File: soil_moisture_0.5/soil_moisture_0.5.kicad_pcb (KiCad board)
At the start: 2 copper layers, 10 parts, among them J1 PPTC021LFBN-RC, J2 1725698, Q1 FDP7030BL, U1 RS_MINI_ULTRA_PRO_V3, U2 SD_BREAKOUT_EBAY

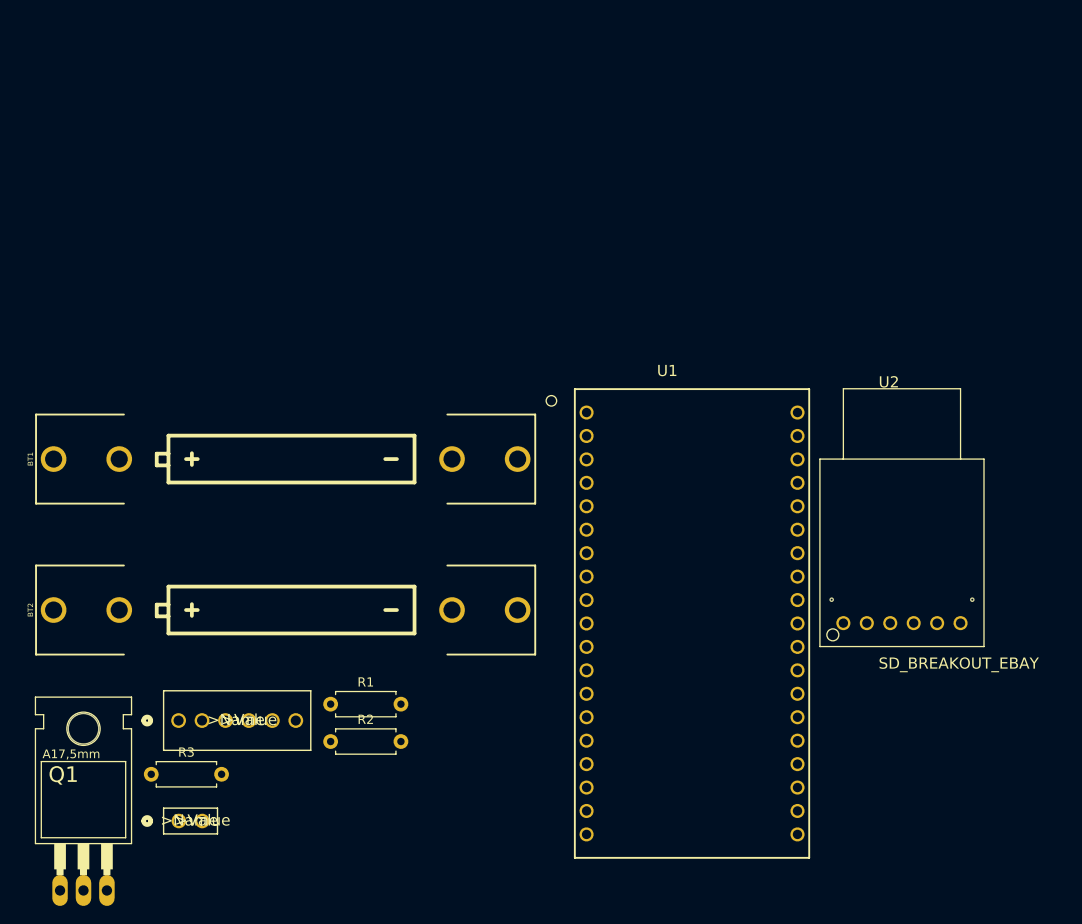
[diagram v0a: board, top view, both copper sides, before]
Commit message: Various hacks - added jumpers for GPIO/A0
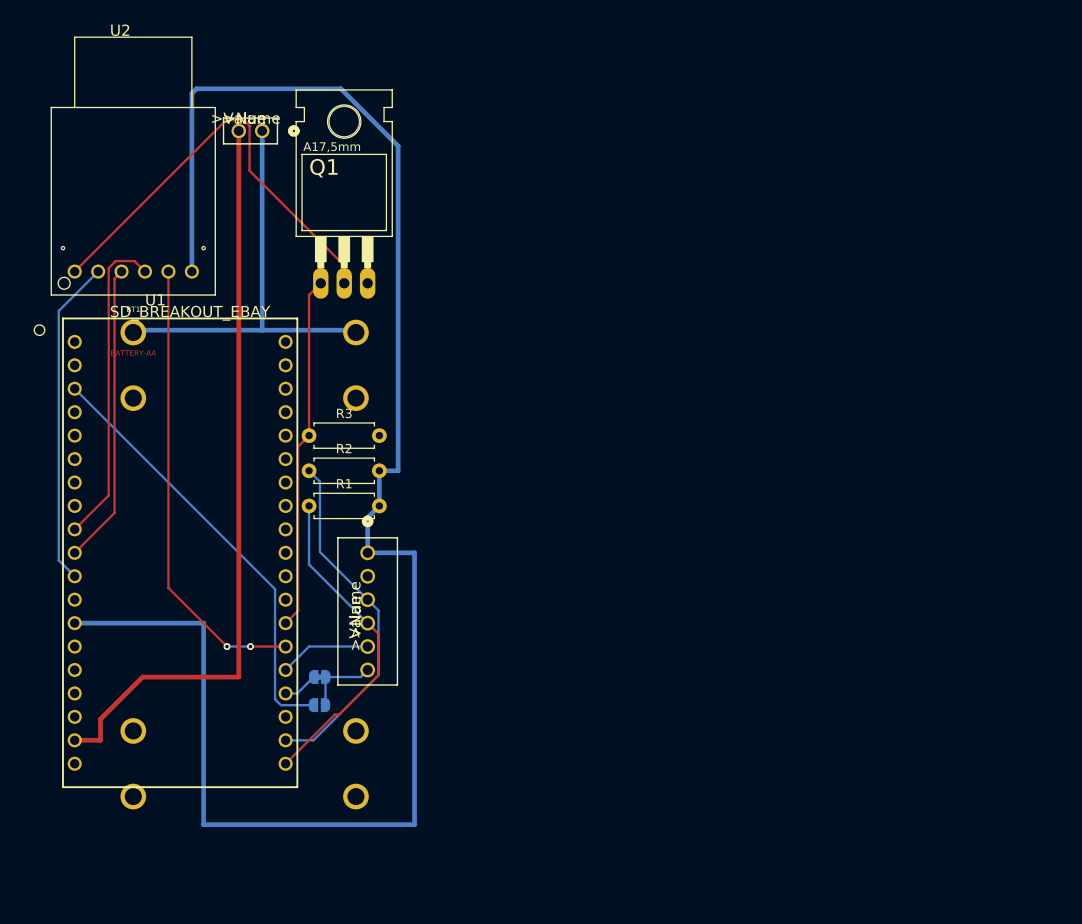
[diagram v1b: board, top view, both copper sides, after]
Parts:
- added JP1: SolderJumper_2_Bridged, Jumper:SolderJumper-2_P1.3mm_Bridged_RoundedPad1.0x1.5mm, B.Cu at (157.4, 110.0)
- added JP2: SolderJumper_2_Open, Jumper:SolderJumper-2_P1.3mm_Open_RoundedPad1.0x1.5mm, B.Cu at (157.3, 113.0)
- BT1, BT2: moved to B.Cu
- moved U2 91.6 mm to (138.4, 66.0)
- moved J1 75.3 mm to (151.1, 50.8), turned to 180 degrees
- moved Q1 71.6 mm to (160.0, 61.0)
- moved U1 56.0 mm to (142.2, 96.5)
- moved R3 40.5 mm to (156.2, 83.8)
- moved R2 29.4 mm to (156.2, 87.6)
- moved J2 27.4 mm to (162.6, 96.5), turned to 270 degrees
- moved R1 21.6 mm to (156.2, 91.4)
- moved BT1 20.1 mm to (137.2, 97.8), turned to 270 degrees
- moved BT2 9.08 mm to (161.3, 97.8), turned to 270 degrees
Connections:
- J2 pad 5: Net-(J2-Pad5) -> GPIO11
- U1 pad 23: Net-(U1-Pad23) -> GPIO12
- U1 pad 24: Net-(U1-Pad24) -> GPIO11
- U1 pad 3: Net-(U1-Pad3) -> A0
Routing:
- net 3V3: track 0.00 -> 184.3 mm
- net BAT: track 0.00 -> 81.1 mm
- net SS: track 0.00 -> 49.6 mm, vias 0 -> 2
- net Net-(BT1-PadPWR@1): track 0.00 -> 47.7 mm
- net Net-(Q1-Pad2): track 0.00 -> 47.3 mm
- net A0: track 0.00 -> 47.1 mm
- net Net-(Q1-Pad1): track 0.00 -> 38.4 mm
- net SCL: track 0.00 -> 38.3 mm
- net SDA: track 0.00 -> 35.5 mm
- net MISO: track 0.00 -> 35.5 mm
- net MOSI: track 0.00 -> 34.6 mm
- net SCK: track 0.00 -> 32.6 mm
- net GPIO11: track 0.00 -> 9.94 mm
- net Net-(J2-Pad6): track 0.00 -> 7.92 mm
- net GPIO12: track 0.00 -> 3.78 mm
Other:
- net class 3V3 added: clearance 0.254, trace_width 0.508, via_dia 0.762, via_drill 0.381
- net class Default: clearance 0.1524 -> 0.254; trace_width 0.1524 -> 0.254; via_dia 0.508 -> 0.762; via_drill 0.254 -> 0.381
- rule trace_clearance: 0.1524 -> 0.254
- rule via_min_drill: 0.254 -> 0.3302
- rule via_min_size: 0.508 -> 0.6858

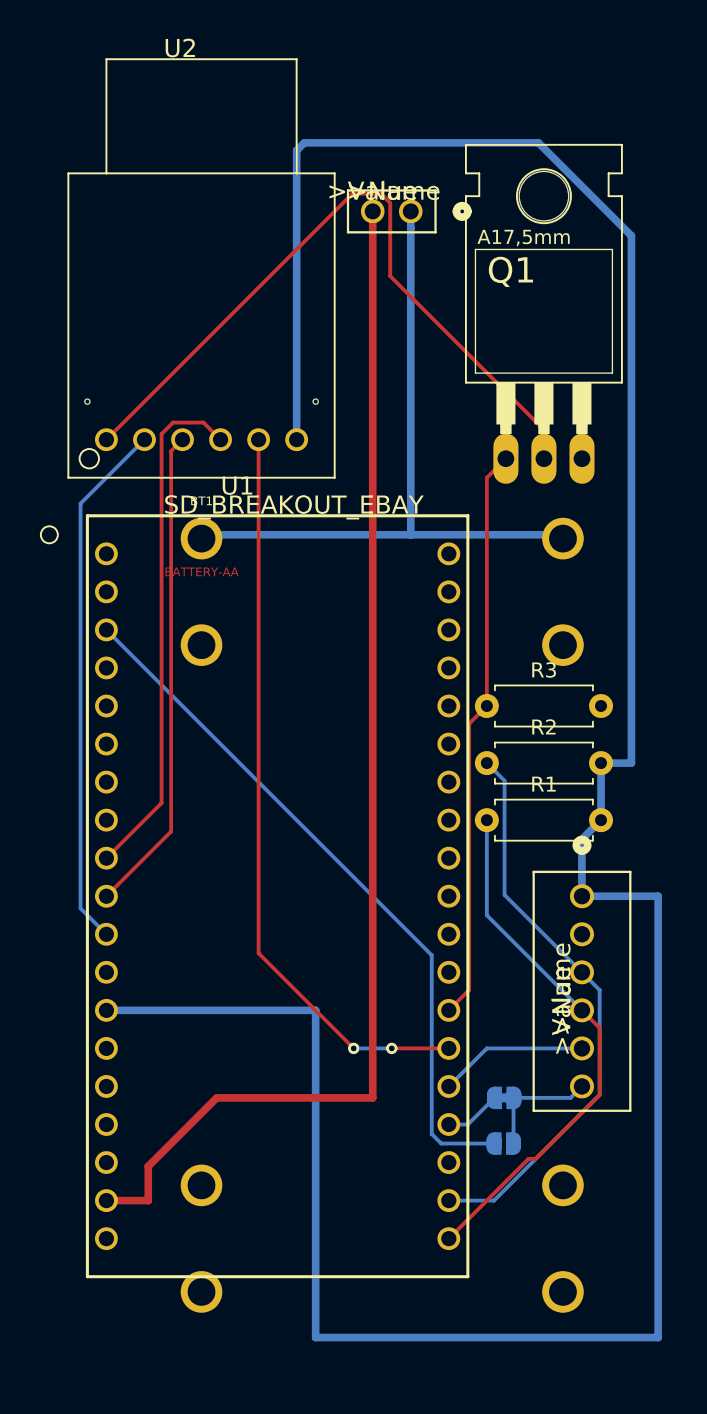
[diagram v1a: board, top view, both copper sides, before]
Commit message: Added second voltage divider for Vbat; board outline
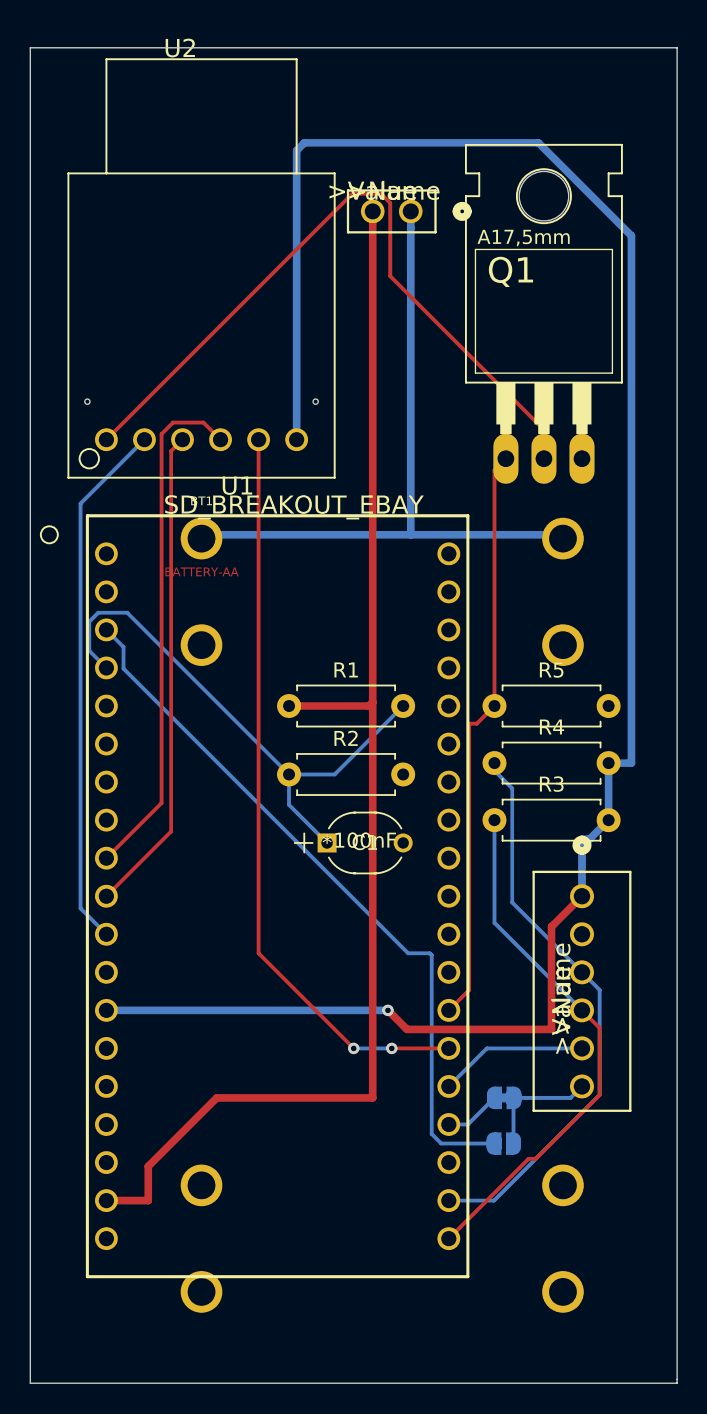
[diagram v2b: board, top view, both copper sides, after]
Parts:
- added C1: 100nF, footprints:C322C104K5R5TA, F.Cu at (145.5, 93.0)
- added R1: 1M, Resistor_THT:R_Axial_DIN0207_L6.3mm_D2.5mm_P7.62mm_Horizontal, F.Cu at (143.0, 83.8)
- added R2: 1M, Resistor_THT:R_Axial_DIN0207_L6.3mm_D2.5mm_P7.62mm_Horizontal, F.Cu at (143.0, 88.4)
- R3: renamed from R1; value R -> 10k
- R4: renamed from R2; value R -> 10k
- R5: renamed from R3; value R -> 10k
- moved R3 0.51 mm to (156.7, 91.4)
- moved R4 0.51 mm to (156.7, 87.6)
- moved R5 0.51 mm to (156.7, 83.8)
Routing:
- net 3V3: track 184.3 -> 131.1 mm, vias 0 -> 1
- net Net-(C1-Pad1): track 0.00 -> 36.8 mm
- net BAT: track 81.1 -> 86.8 mm
- net A0: track 47.1 -> 47.9 mm
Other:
- board outline added: 43.2 x 89.2 mm

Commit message: Added Gerbers and a BOM
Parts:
- added H1: MountingHole, MountingHole:MountingHole_4.3mm_M4, F.Cu at (147.3, 44.5)
- added H2: MountingHole, MountingHole:MountingHole_4.3mm_M4, F.Cu at (147.3, 124.5)
- moved J1 3.30 mm to (151.1, 54.1)
- moved U2 1.80 mm to (136.7, 66.3)
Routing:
- net 3V3: track 131.1 -> 124.1 mm
- net Net-(BT1-PadPWR@1): track 47.7 -> 44.2 mm
- net BAT: track 86.8 -> 83.8 mm
- net Net-(Q1-Pad2): track 47.3 -> 46.0 mm
- net MOSI: track 34.6 -> 33.5 mm
- net SCK: track 32.6 -> 31.6 mm
- net MISO: track 35.5 -> 34.5 mm
- added copper zone on B.Cu, net GND
- added copper zone on F.Cu, net GND
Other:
- board text added: "+"
- board text added: "-"
- board text added: "G11"
- board text added: "G12 A0"
- board text added: "J1"
- board text added: "J2"
- board text added: "James Gallagher HAST Leaf Node 0.5"
- board text added: "Power"
- board text added: "SCL"
- board text added: "SDA"
